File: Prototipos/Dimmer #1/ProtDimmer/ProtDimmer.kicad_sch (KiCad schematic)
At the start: 16 parts, among them K1 SRD-05VDC-SL-C, Q1 BC548B, Q3 BT137, U1 EL817, U3 MOC3021M

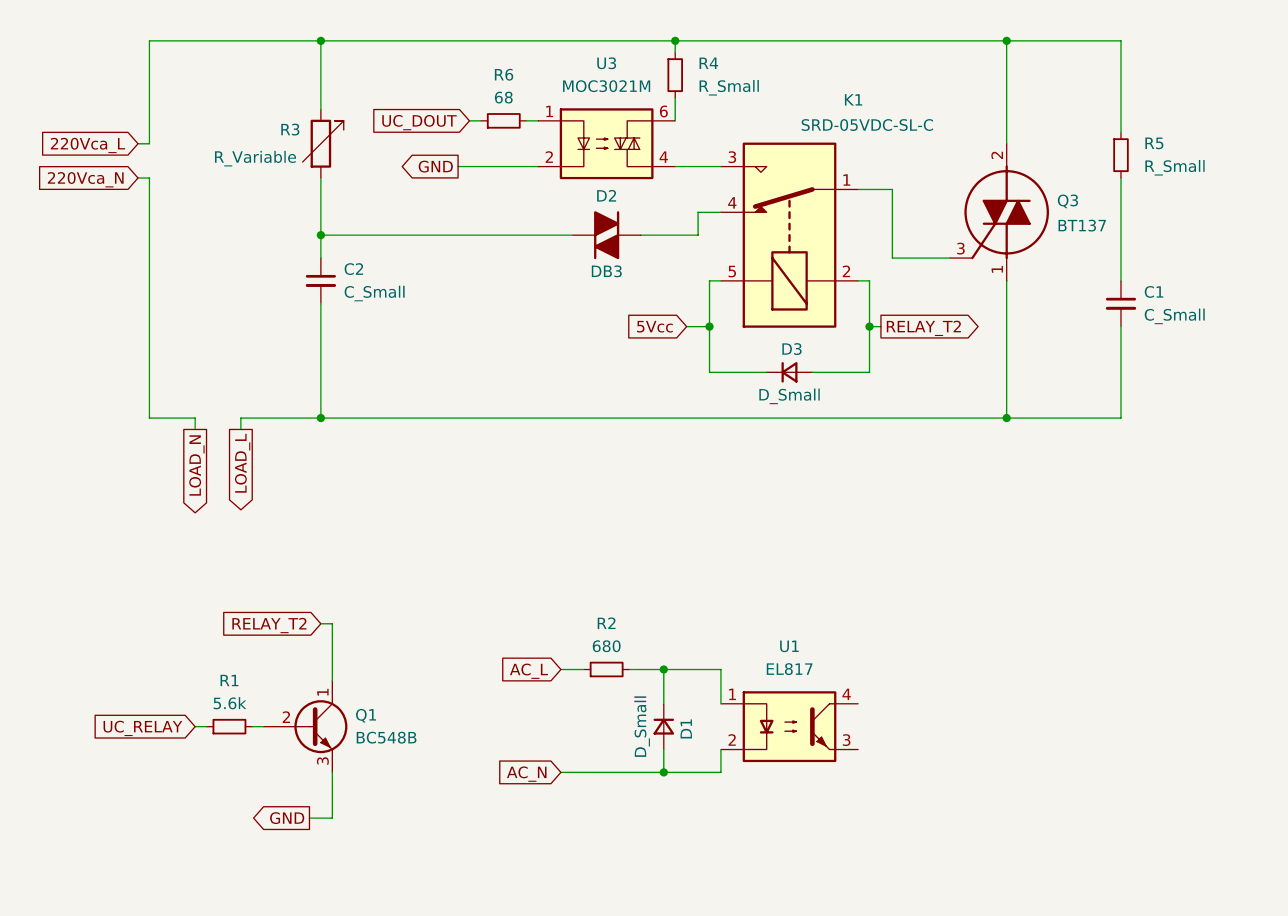
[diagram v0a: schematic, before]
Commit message: Primeros ajustes para adaptar a 48 Vac
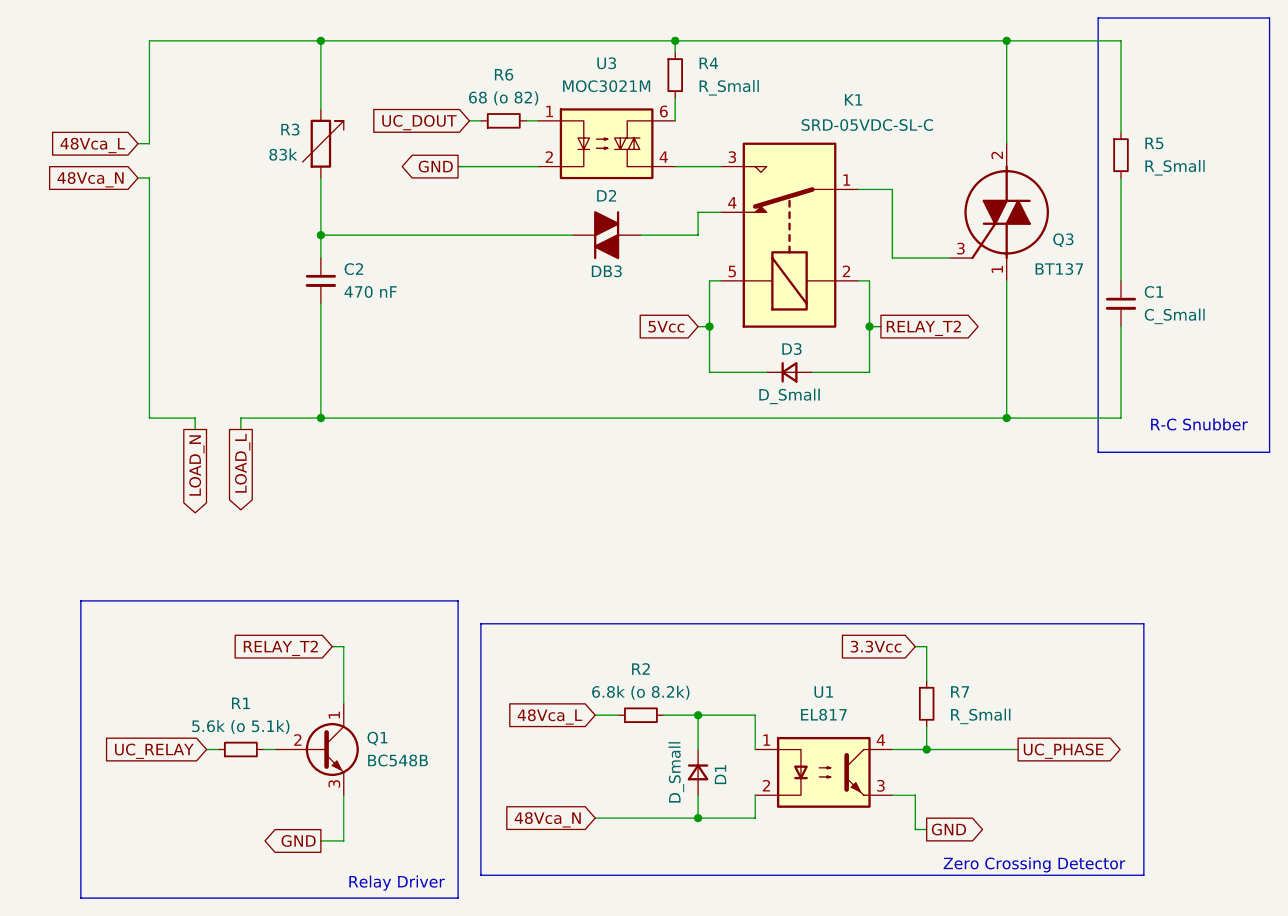
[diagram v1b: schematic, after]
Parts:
- added R7: R_Small, symbol Device:R_Small
- C2: value C_Small -> 470 nF
- R1: value 5.6k -> 5.6k (o 5.1k)
- R2: value 680 -> 6.8k (o 8.2k)
- R3: value R_Variable -> 83k
- R6: value 68 -> 68 (o 82)
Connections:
- net AC_L is gone; now on net 48Vca_L: R2.1
- net GND: now also U1.3
- net UC_PHASE: now reaches U1.4
- net UC_PHASE: now also R7.2
- net 220Vca_L renamed 48Vca_L
- net AC_N renamed 48Vca_N
- new net 3.3Vcc: R7.1
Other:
- note added: "R-C Snubber"
- note added: "Relay Driver"
- note added: "Zero Crossing Detector"
- moved on the sheet: D1, Q1, R1, R2, U1

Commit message: Modificaciones circuito
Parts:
- added R8: 150k, symbol Device:R_Small
- added R9: 1k, symbol Device:R_Small
- C1: value C_Small -> 0.01uF
- C2: value 470 nF -> 100 nF
- R3: value 83k -> 100k
- R5: value R_Small -> 39
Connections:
- net 48Vca_L: now also R8.1
- net at C2.1, D2.1 (K): now also R9.2; no longer R3.2
- new net: R3.2, R8.2, R9.1
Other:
- moved on the sheet: C2, R3

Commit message: Agregar valores componentes, eliminar contenido de otras tareas
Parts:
- C1: renamed from C2; value 100 nF -> 100nF
- C2: renamed from C1; value 0.01uF -> 10nF
- R2: renamed from R1; value 5.6k (o 5.1k) -> 12k
- R5: renamed from R6; value 68 (o 82) -> 82
- R6: renamed from R2; value 6.8k (o 8.2k) -> 1.8k
- R7: renamed from R4; value R_Small -> 82
- R8: renamed from R7; value R_Small -> 10k
- R9: renamed from R5; value 39 -> 51
- renumbered D2 to D1, D1 to D2, Q3 to Q2, R8 to R1, R9 to R4, U3 to U1, U1 to U2
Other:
- moved on the sheet: D1
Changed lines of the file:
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@@
 	(wire
 		(pts
-			(xy 91.44 46.99) (xy 85.09 46.99)
+			(xy 91.44 48.26) (xy 85.09 48.26)
 		)
 		(stroke
@@
 	(wire
 		(pts
-			(xy 46.99 53.34) (xy 77.47 53.34)
+			(xy 46.99 53.34) (xy 71.12 53.34)
 		)
 		(stroke
@@
 	(wire
 		(pts
-			(xy 91.44 44.45) (xy 91.44 46.99)
+			(xy 91.44 44.45) (xy 91.44 48.26)
 		)
 		(stroke
@@
 	(wire
 		(pts
-			(xy 77.47 53.34) (xy 77.47 46.99)
+			(xy 71.12 48.26) (xy 71.12 53.34)
 		)
 		(stroke
@@
 		(pts
 			(xy 38.1 39.37) (xy 38.1 41.91)
+		)
+		(stroke
+			(width 0)
+			(type default)
+		)
+	)
+	(wire
+		(pts
+			(xy 71.12 48.26) (xy 77.47 48.26)
 		)
 		(stroke
@@
 		(dnp no)
 		(fields_autoplaced yes)
-		(property "Reference" "R5"
+		(property "Reference" "R9"
 			(at 140.97 36.8299 0)
 			(effects
@@
 			)
 		)
-		(property "Value" "39"
+		(property "Value" "51"
 			(at 140.97 39.3699 0)
 			(effects
@@
 			(project "ProtDimmer"
 				(path "/0b9ede13-5f58-4dce-901a-9d27a513b221"
-					(reference "R5")
+					(reference "R9")
 					(unit 1)
 				)
@@
 		(dnp no)
 		(fields_autoplaced yes)
-		(property "Reference" "C2"
+		(property "Reference" "C1"
 			(at 49.53 58.4262 0)
 			(effects
@@
 			)
 		)
-		(property "Value" "100 nF"
+		(property "Value" "100nF"
 			(at 49.53 60.9662 0)
 			(effects
@@
 			(project "ProtDimmer"
 				(path "/0b9ede13-5f58-4dce-901a-9d27a513b221"
-					(reference "C2")
+					(reference "C1")
 					(unit 1)
 				)
@@
 		(dnp no)
 		(fields_autoplaced yes)
-		(property "Reference" "U1"
+		(property "Reference" "U2"
 			(at 105.41 97.79 0)
 			(effects
@@
 			(project ""
 				(path "/0b9ede13-5f58-4dce-901a-9d27a513b221"
-					(reference "U1")
+					(reference "U2")
 					(unit 1)
 				)
@@
 	(symbol
 		(lib_id "Device:DIAC")
-		(at 81.28 46.99 0)
+		(at 81.28 48.26 0)
 		(unit 1)
 		(exclude_from_sim no)
@@
 		(on_board yes)
 		(dnp no)
-		(property "Reference" "D2"
-			(at 81.28 42.672 0)
+		(property "Reference" "D1"
+			(at 81.28 43.942 0)
 			(effects
 				(font
@@
 		)
 		(property "Value" "DB3"
-			(at 81.28 51.054 0)
+			(at 81.28 52.324 0)
 			(effects
 				(font
@@
 		)
 		(property "Footprint" ""
-			(at 81.28 46.99 0)
+			(at 81.28 48.26 0)
 			(effects
 				(font
@@
 		)
 		(property "Datasheet" "~"
-			(at 81.28 46.99 0)
+			(at 81.28 48.26 0)
 			(effects
 				(font
@@
 		)
 		(property "Description" "Diode for alternating current"
-			(at 81.28 46.99 0)
+			(at 81.28 48.26 0)
 			(effects
 				(font
@@
 			(project "ProtDimmer"
 				(path "/0b9ede13-5f58-4dce-901a-9d27a513b221"
-					(reference "D2")
+					(reference "D1")
 					(unit 1)
 				)
@@
 		(dnp no)
 		(fields_autoplaced yes)
-		(property "Reference" "U3"
+		(property "Reference" "U1"
 			(at 81.28 27.94 0)
 			(effects
@@
 			(project "ProtDimmer"
 				(path "/0b9ede13-5f58-4dce-901a-9d27a513b221"
-					(reference "U3")
+					(reference "U1")
 					(unit 1)
 				)
@@
 		(on_board yes)
 		(dnp no)
-		(property "Reference" "R9"
+		(property "Reference" "R4"
 			(at 49.276 46.0285 0)
 			(effects
@@
 			(project "ProtDimmer"
 				(path "/0b9ede13-5f58-4dce-901a-9d27a513b221"
-					(reference "R9")
+					(reference "R4")
 					(unit 1)
 				)
@@
 		(on_board yes)
 		(dnp no)
-		(property "Reference" "R1"
+		(property "Reference" "R2"
 			(at 40.64 99.06 90)
 			(effects
@@
 			)
 		)
-		(property "Value" "5.6k (o 5.1k)"
+		(property "Value" "12k"
 			(at 40.64 101.6 90)
 			(effects
@@
 			(project ""
 				(path "/0b9ede13-5f58-4dce-901a-9d27a513b221"
-					(reference "R1")
+					(reference "R2")
 					(unit 1)
 				)
@@
 		(dnp no)
 		(fields_autoplaced yes)
-		(property "Reference" "C1"
+		(property "Reference" "C2"
 			(at 140.97 53.3462 0)
 			(effects
@@
 			)
 		)
-		(property "Value" "0.01uF"
+		(property "Value" "10nF"
 			(at 140.97 55.8862 0)
 			(effects
@@
 			(project "ProtDimmer"
 				(path "/0b9ede13-5f58-4dce-901a-9d27a513b221"
-					(reference "C1")
+					(reference "C2")
 					(unit 1)
 				)
@@
 		(dnp no)
 		(fields_autoplaced yes)
-		(property "Reference" "R4"
+		(property "Reference" "R7"
 			(at 91.44 27.9399 0)
 			(effects
@@
 			)
 		)
-		(property "Value" "R_Small"
+		(property "Value" "82"
 			(at 91.44 30.4799 0)
 			(effects
@@
 			(project "ProtDimmer"
 				(path "/0b9ede13-5f58-4dce-901a-9d27a513b221"
-					(reference "R4")
+					(reference "R7")
 					(unit 1)
 				)
@@
 		(dnp no)
 		(fields_autoplaced yes)
-		(property "Reference" "R7"
+		(property "Reference" "R8"
 			(at 119.38 97.7899 0)
 			(effects
@@
 			)
 		)
-		(property "Value" "R_Small"
+		(property "Value" "10k"
 			(at 119.38 100.3299 0)
 			(effects
@@
 			(project "ProtDimmer"
 				(path "/0b9ede13-5f58-4dce-901a-9d27a513b221"
-					(reference "R7")
+					(reference "R8")
 					(unit 1)
 				)
@@
 		(dnp no)
 		(fields_autoplaced yes)
-		(property "Reference" "R6"
+		(property "Reference" "R5"
 			(at 69.85 29.21 90)
 			(effects
@@
 			)
 		)
-		(property "Value" "68 (o 82)"
+		(property "Value" "82"
 			(at 69.85 31.75 90)
 			(effects
@@
 			(project "ProtDimmer"
 				(path "/0b9ede13-5f58-4dce-901a-9d27a513b221"
-					(reference "R6")
+					(reference "R5")
 					(unit 1)
 				)
@@
 		(on_board yes)
 		(dnp no)
-		(property "Reference" "R8"
+		(property "Reference" "R1"
 			(at 40.386 35.814 0)
 			(effects
@@
 			(project ""
 				(path "/0b9ede13-5f58-4dce-901a-9d27a513b221"
-					(reference "R8")
+					(reference "R1")
 					(unit 1)
 				)
@@
 		(on_board yes)
 		(dnp no)
-		(property "Reference" "Q3"
+		(property "Reference" "Q2"
 			(at 130.81 47.498 90)
 			(effects
@@
 			(project "ProtDimmer"
 				(path "/0b9ede13-5f58-4dce-901a-9d27a513b221"
-					(reference "Q3")
+					(reference "Q2")
 					(unit 1)
 				)
@@
 		(dnp no)
 		(fields_autoplaced yes)
-		(property "Reference" "R2"
+		(property "Reference" "R6"
 			(at 85.09 95.25 90)
 			(effects
@@
 			)
 		)
-		(property "Value" "6.8k (o 8.2k)"
+		(property "Value" "1.8k"
 			(at 85.09 97.79 90)
 			(effects
@@
 			(project "ProtDimmer"
 				(path "/0b9ede13-5f58-4dce-901a-9d27a513b221"
-					(reference "R2")
+					(reference "R6")
 					(unit 1)
 				)
@@
 		(on_board yes)
 		(dnp no)
-		(property "Reference" "D1"
+		(property "Reference" "D2"
 			(at 93.98 106.934 0)
 			(effects
@@
 			(project "ProtDimmer"
 				(path "/0b9ede13-5f58-4dce-901a-9d27a513b221"
-					(reference "D1")
+					(reference "D2")
 					(unit 1)
 				)
